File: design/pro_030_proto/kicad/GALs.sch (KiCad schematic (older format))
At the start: 6 parts, among them IC2 ATF22V10C

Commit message: Add interrupt glue to schematic
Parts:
- removed C? (x2): 100nF, rosco_m68k:C2.5-3, symbol rosco_m68k-eagle-import:C2,5-3
- removed IC? (x2): ATF16V8BQL-15PU, rosco_m68k:DIL20, symbol rosco_m68k-eagle-import:ATF16V8BP3
- removed R?: 2K2, rosco_m68k:0207_10, symbol rosco_m68k-eagle-import:R-EU_0207_10
- added C? (x3): 100nF, Capacitor_THT:C_Rect_L4.0mm_W2.5mm_P2.50mm, symbol rosco_m68k-eagle-import:C2,5-3
- added IC3, IC?: ATF22V10C, Package_DIP:DIP-24_W7.62mm_Socket_LongPads, symbol rosco_m68k:GAL22V10
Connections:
- net labels added: A0, A1, A2, A3, ANYIACK, DSA0, DSA1, IACK1, IACK2, IACK3, IACK4, IACK5, IACK6, IACK7, RAMEN0, RAMEN1, RAMEN2, RAMEN3, ROMEN0, ROMEN1, ROMEN2, ROMEN3, RnW, SIZ0, SIZ1, WR
- net labels removed: A[1..23], BOOT, DTACK, EVENRAMSEL, EVENROMSEL, EXPSEL, IACK, IODTACK, IOSEL, LDS, MFPDS, ODDRAMSEL, ODDROMSEL, RAMOE, UDS
- wire segments 28 -> 21
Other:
- note added: "IC3_MEM_SELECTS.PLD"
- note added: "IC4_INTERRUPT_GLUE.PLD"
- note removed: "GLUE_LOGIC.PLD"

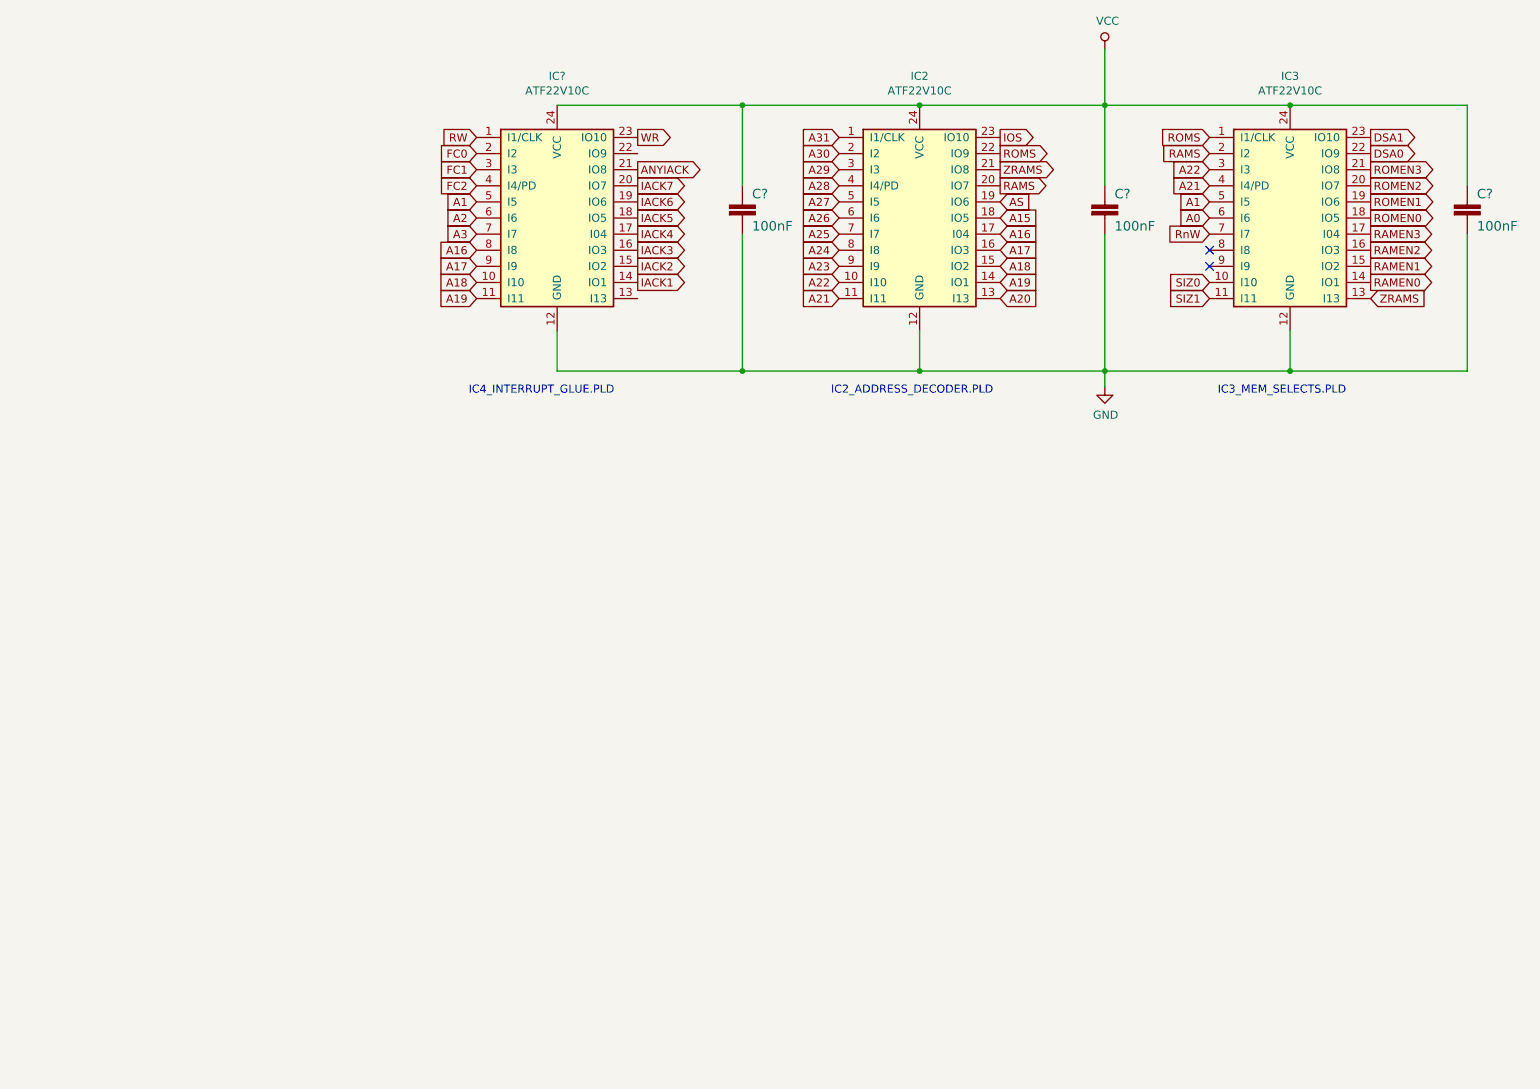
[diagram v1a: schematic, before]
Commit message: Largeish changeset:
* Added (first-cut) glue for DTACK generation
* Fix mem selects to use new DTACK generation
* Add missing footprints for Kicad
* Add POWER and TESTPOINTS schematics
* Update footprints across the board to allow error-free PCB import
* Pull all components (so far) into PCB
* Fix MC68030RC footprint (missing pads)
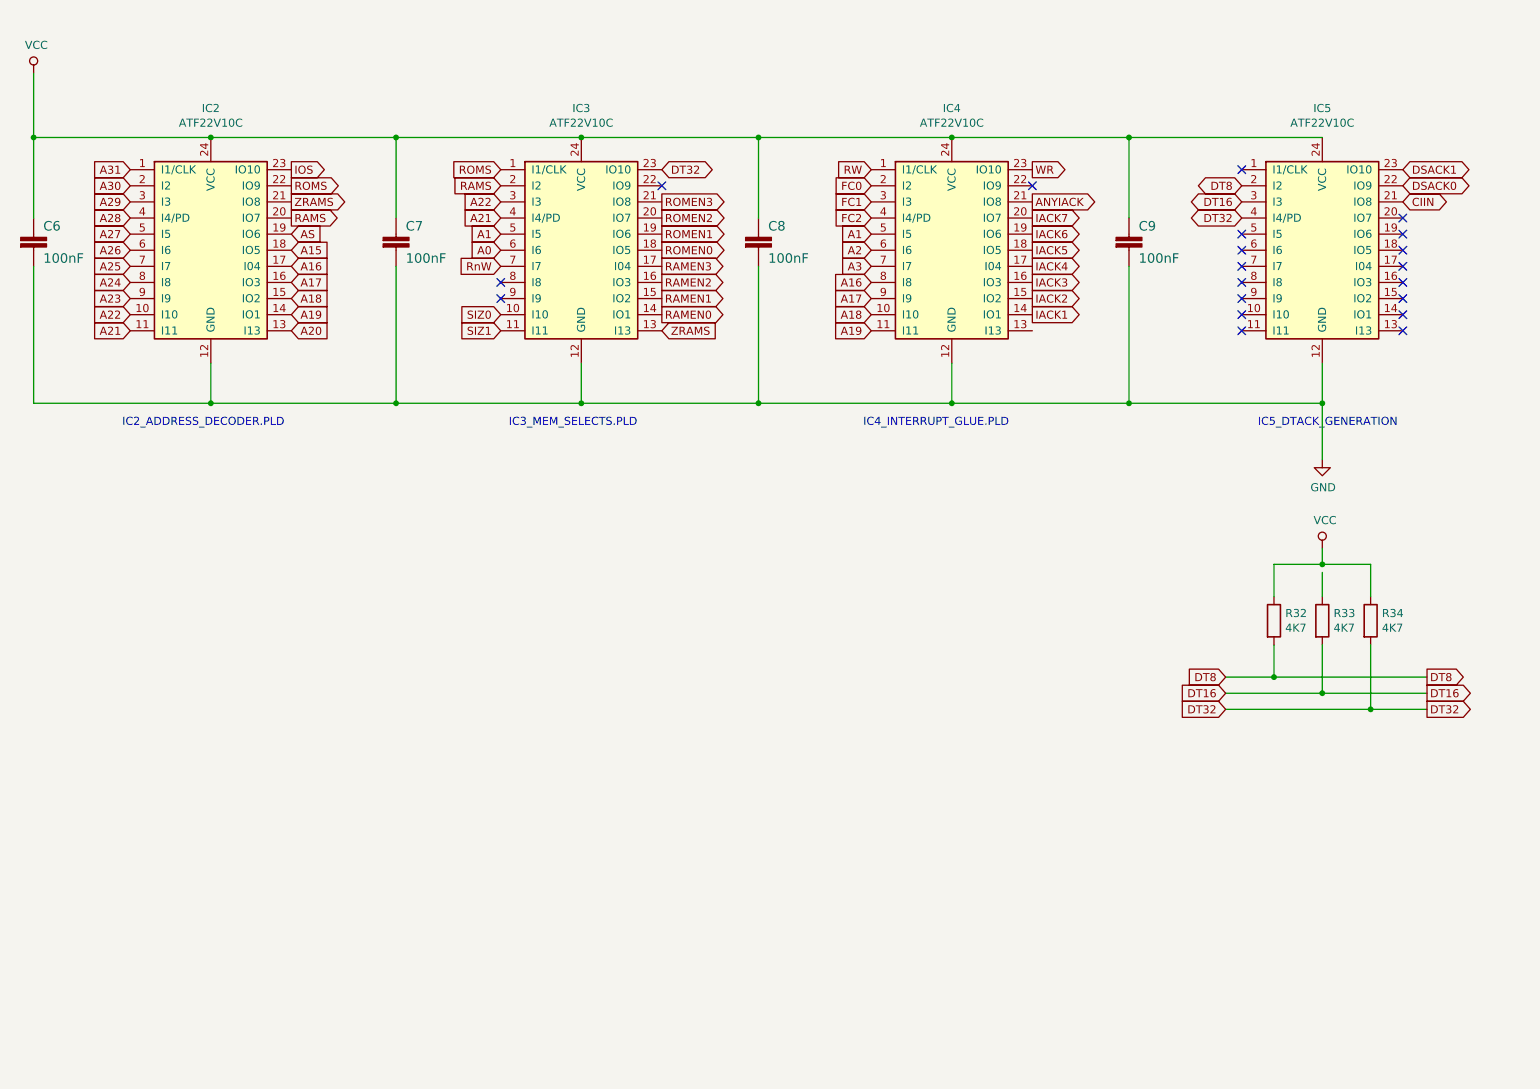
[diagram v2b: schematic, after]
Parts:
- added C9: 100nF, Capacitor_THT:C_Rect_L4.0mm_W2.5mm_P2.50mm, symbol rosco_m68k-eagle-import:C2,5-3
- added IC5: ATF22V10C, Package_DIP:DIP-24_W7.62mm_Socket_LongPads, symbol rosco_m68k:GAL22V10
- added R32, R33, R34: 4K7, rosco_m68k:R-0207_10, symbol Device:R
- gave numbers to parts that had none: 4
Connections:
- net GND: now also C9.2, IC5.12 (GND)
- net VCC: now also C9.1, IC5.24 (VCC), R32.1, R34.1
- net DSA0: no longer names the net of IC3.22 (IO9)
- net DSA1 renamed DT32
- net DT32: now also IC5.4 (I4/PD), R34.2
- new net CIIN: IC5.21 (IO8)
- new net DSACK0: IC5.22 (IO9)
- new net DSACK1: IC5.23 (IO10)
- new net DT16: IC5.3 (I3), R33.2
- new net DT8: IC5.2 (I2), R32.2
- no-connect marks 2 -> 20
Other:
- note added: "IC5_DTACK_GENERATION"
- moved on the sheet: C6, C7, C8, IC2, IC3, IC4

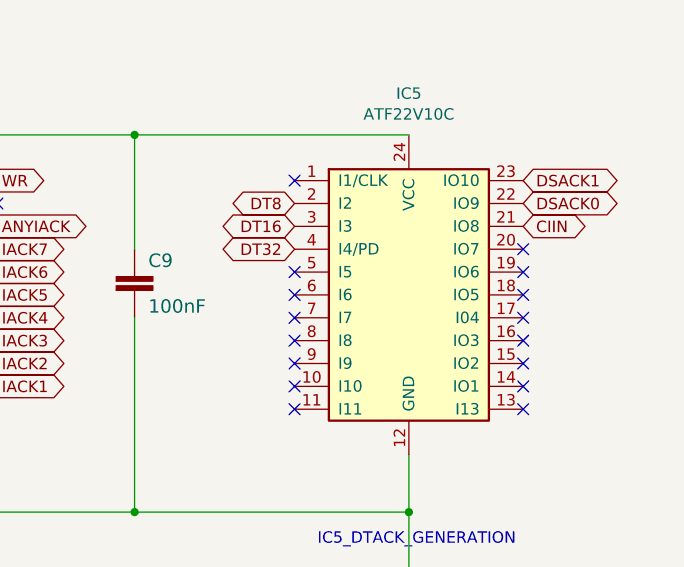
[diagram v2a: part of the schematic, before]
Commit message: Add DTACK delays and fixes
* Add configurable DTACK delay for RAM & ROM
* Add DTACK generation for RAM/ROM with delay support in IC5
* Fix /BOOT line generator for 32-bit port
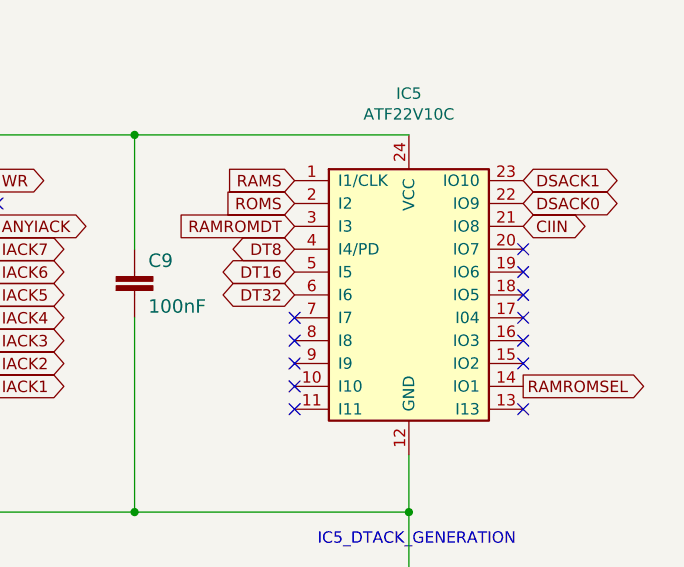
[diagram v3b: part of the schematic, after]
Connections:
- net DT16: now also IC5.5 (I5); no longer IC5.3 (I3)
- net DT32: now also IC5.6 (I6); no longer IC5.4 (I4/PD)
- net DT8: now also IC5.4 (I4/PD); no longer IC5.2 (I2)
- net RAMS: now also IC5.1 (I1/CLK)
- net ROMS: now also IC5.2 (I2)
- net RAMROMSEL: now reaches IC5.14 (IO1)
- new net RAMROMDT: IC5.3 (I3)
- no-connect marks 20 -> 16
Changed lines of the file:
@@
 DSACK0
 NoConn ~ 9800 2050
-Text GLabel 8800 1850 0    50   3State ~ 0
+Text GLabel 8800 2050 0    50   3State ~ 0
 DT8
-Text GLabel 8800 1950 0    50   3State ~ 0
+Text GLabel 8800 2150 0    50   3State ~ 0
 DT16
-Text GLabel 8800 2050 0    50   3State ~ 0
+Text GLabel 8800 2250 0    50   3State ~ 0
 DT32
 NoConn ~ 5200 1850
@@
 NoConn ~ 9800 2450
 NoConn ~ 9800 2550
-NoConn ~ 9800 2650
 NoConn ~ 9800 2750
-NoConn ~ 8800 2150
-NoConn ~ 8800 1750
-NoConn ~ 8800 2250
 NoConn ~ 8800 2350
 NoConn ~ 8800 2450
@@
 Wire Wire Line
 	9600 5100 9950 5100
+Text GLabel 8800 1750 0    50   Input ~ 0
+RAMS
+Text GLabel 8800 1850 0    50   Input ~ 0
+ROMS
+Text GLabel 8800 1950 0    50   Input ~ 0
+RAMROMDT
+Text GLabel 9800 2650 2    50   Output ~ 0
+RAMROMSEL
 $EndSCHEMATC
